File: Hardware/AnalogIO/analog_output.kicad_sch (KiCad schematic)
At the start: 18 parts, among them U23 MCP6002-xSN, U24 MCP6002-xSN, U4 MCP6002-xSN, U5 MCP6002-xSN

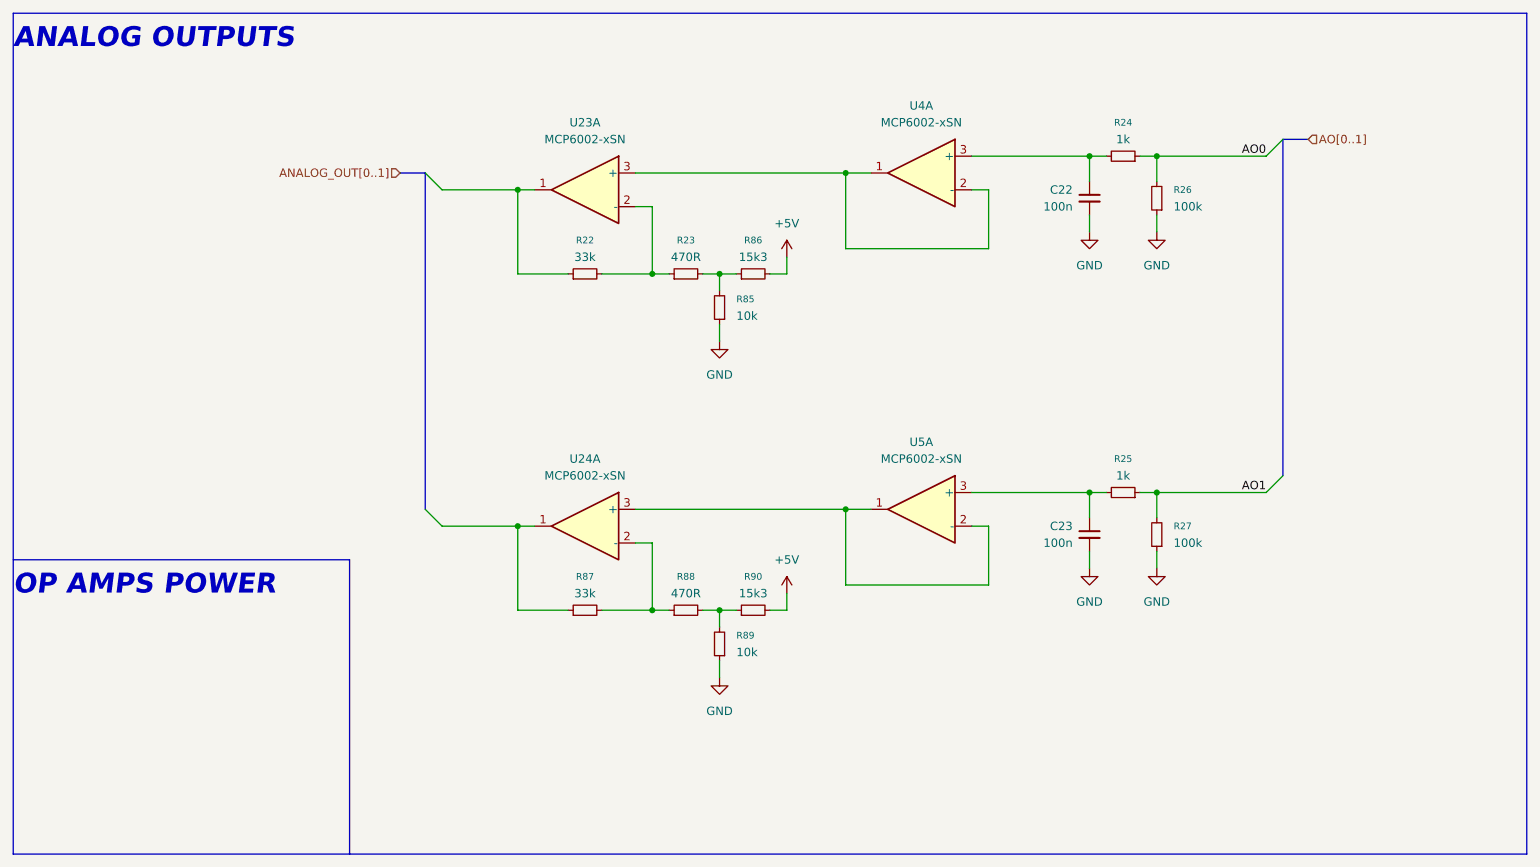
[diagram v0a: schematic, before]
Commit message: schematic update - all pcbs
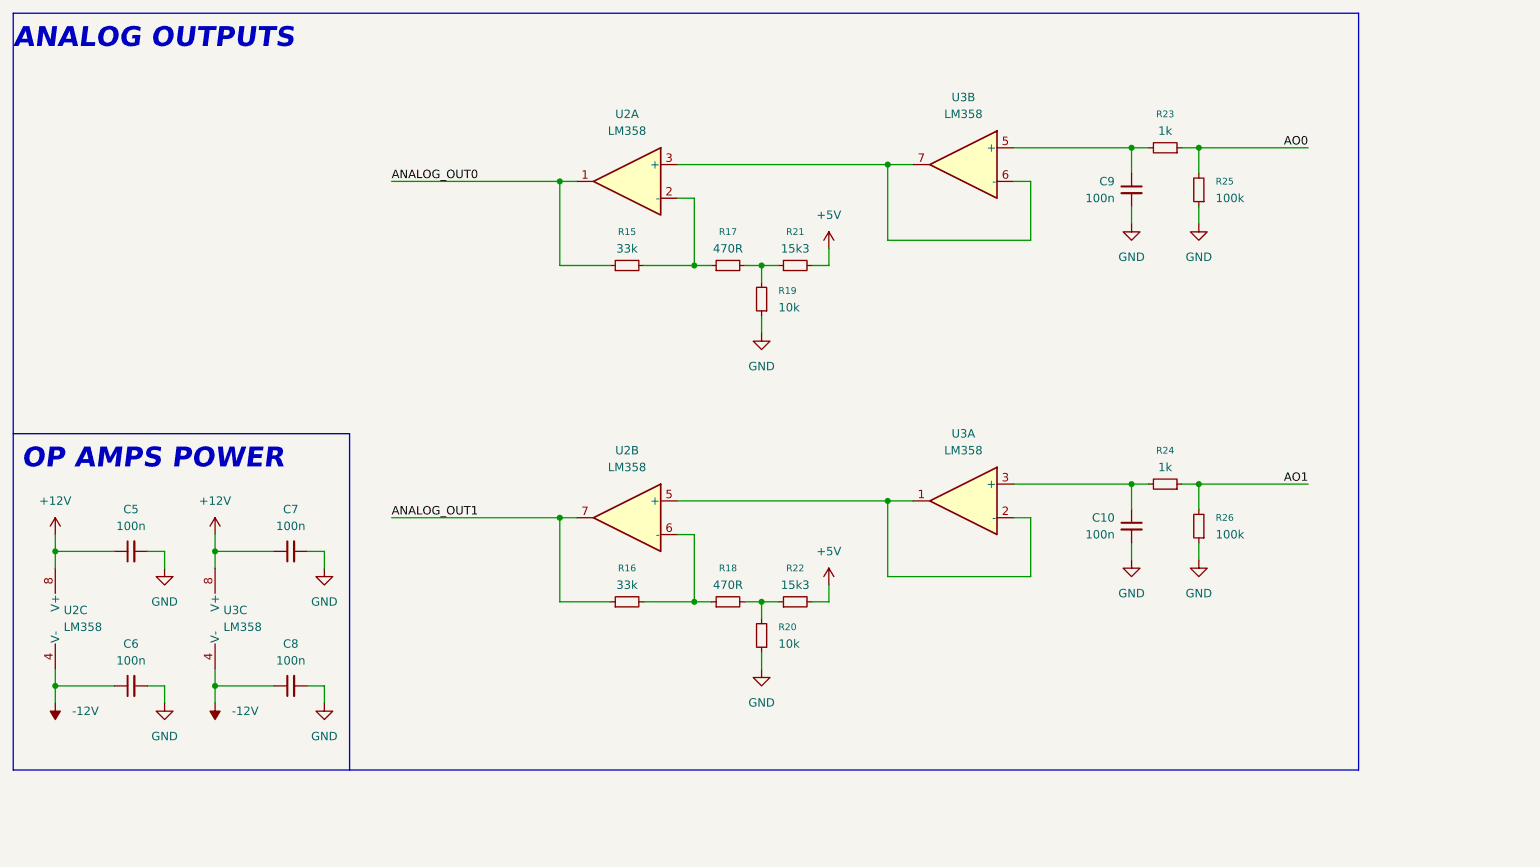
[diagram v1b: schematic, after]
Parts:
- removed U23, U24, U4: MCP6002-xSN, Package_SO:SOIC-8_3.9x4.9mm_P1.27mm, symbol Amplifier_Operational:MCP6002-xSN
- removed U5: MCP6002-xSN, symbol Amplifier_Operational:MCP6002-xSN
- added C5, C6, C7, C8: 100n, symbol Device:C_Small
- added U2, U3: LM358, symbol Amplifier_Operational:LM358
- renumbered C23 to C10, C22 to C9, R22 to R15, R87 to R16, R23 to R17, R88 to R18, R85 to R19, R89 to R20, R86 to R21, R90 to R22, R24 to R23, R25 to R24, R26 to R25, R27 to R26
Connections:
- net GND: now also C5.2, C6.2, C7.2, C8.2
- net at R15.2, R17.1: now also U2.2 (-)
- net ANALOG_OUT0: now reaches R15.1
- net ANALOG_OUT0: now also U2.1
- net at C10.1, R24.2: now also U3.3 (+)
- net at C9.1, R23.2: now also U3.5 (+)
- net ANALOG_OUT1: now reaches R16.1
- net ANALOG_OUT1: now also U2.7
- net at R16.2, R18.1: now also U2.6 (-)
- new net: U2.5 (+), U3.1, U3.2 (-)
- new net: U2.3 (+), U3.6 (-), U3.7
- new net +12V: C5.1, C7.1, U2.8 (V+), U3.8 (V+)
- new net -12V: C6.1, C8.1, U2.4 (V-), U3.4 (V-)
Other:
- moved on the sheet: C10, C9, R15, R16, R17, R18, R19, R20, R21, R22, R23, R24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

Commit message: schematic update - digital and analog footprints added
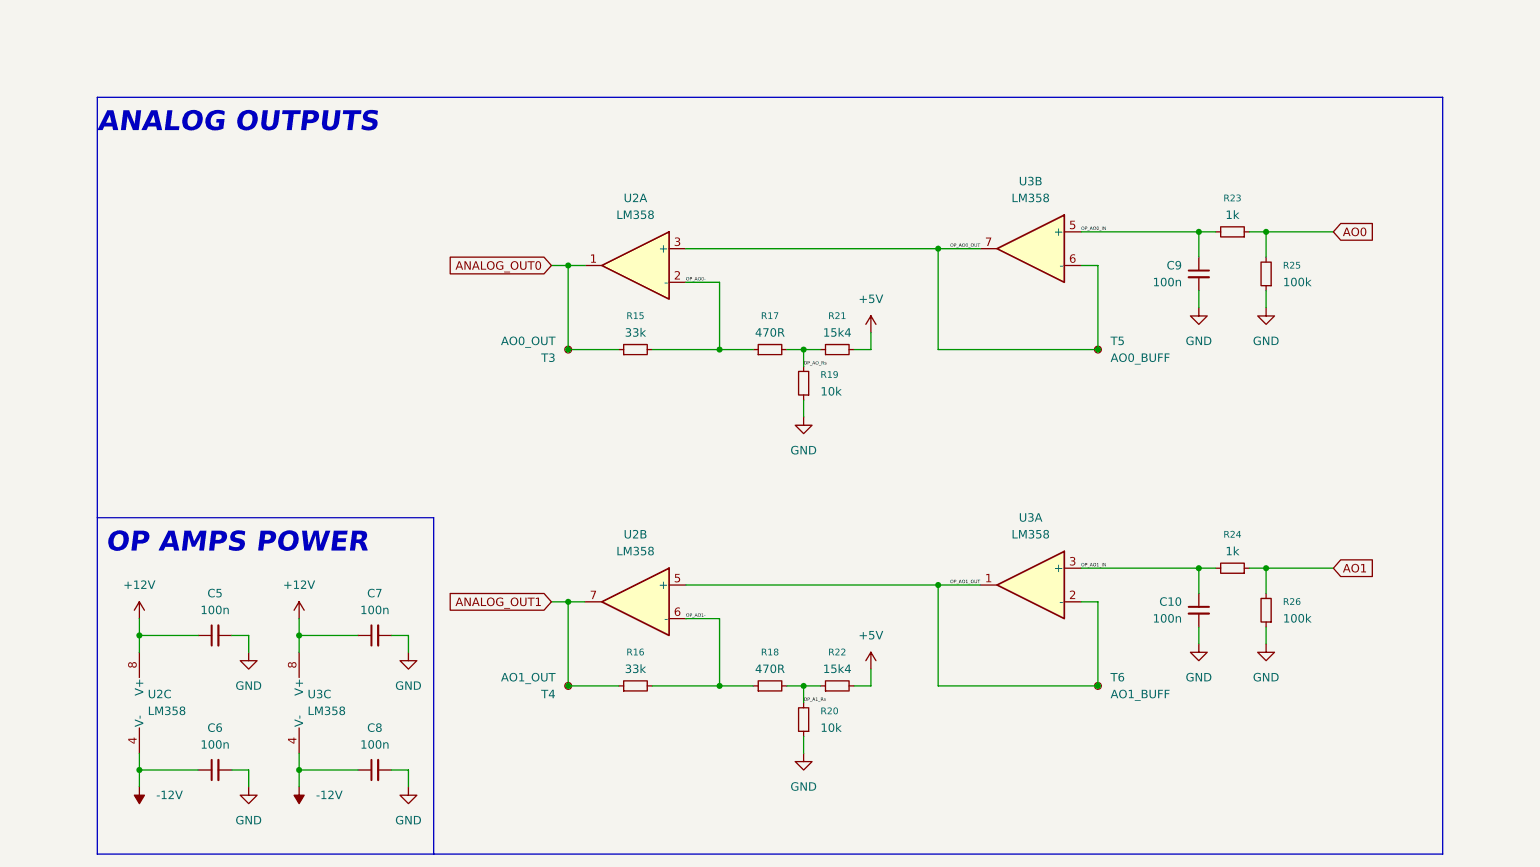
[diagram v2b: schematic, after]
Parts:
- added T3: AO0_OUT, TestPoint:TestPoint_Pad_1.0x1.0mm, symbol Connector:TestPoint_Small
- added T4: AO1_OUT, TestPoint:TestPoint_Pad_1.0x1.0mm, symbol Connector:TestPoint_Small
- added T5: AO0_BUFF, TestPoint:TestPoint_Pad_1.0x1.0mm, symbol Connector:TestPoint_Small
- added T6: AO1_BUFF, TestPoint:TestPoint_Pad_1.0x1.0mm, symbol Connector:TestPoint_Small
- C5, C6, C7, C8: footprint (none) -> Capacitor_SMD:C_0603_1608Metric_Pad1.08x0.95mm_HandSolder; Mouser Part Number (none) -> GRM033R6YA104ME14D; Mouser Price/Stock (none) -> https://www.mouser.pl/ProductDetail/Murata-Electronics/GRM0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
- R15, R16: footprint (none) -> Resistor_SMD:R_0603_1608Metric_Pad0.98x0.95mm_HandSolder; Mouser Part Number (none) -> 71-CRCW0603-33K-E3; Mouser Price/Stock (none) -> https://www.mouser.pl/ProductDetail/Vishay/CRCW060333K0FKEA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
- R17, R18: footprint (none) -> Resistor_SMD:R_0603_1608Metric_Pad0.98x0.95mm_HandSolder; Mouser Part Number (none) -> 71-CRCW0603-470-E3; Mouser Price/Stock (none) -> https://www.mouser.pl/ProductDetail/Vishay/CRCW0603470RFKEA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
- R19, R20: footprint (none) -> Resistor_SMD:R_0603_1608Metric_Pad0.98x0.95mm_HandSolder; Mouser Part Number (none) -> 71-CRCW0603-10K-E3; Mouser Price/Stock (none) -> https://www.mouser.pl/ProductDetail/Vishay/CRCW060310K0FKEA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
- R21, R22: value 15k3 -> 15k4; footprint (none) -> Resistor_SMD:R_0603_1608Metric_Pad0.98x0.95mm_HandSolder; Mouser Part Number (none) -> 71-CRCW0603-15.4K-E3; Mouser Price/Stock (none) -> https://www.mouser.pl/ProductDetail/Vishay/CRCW060315K4FKEA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
- U2, U3: footprint (none) -> Package_SO:SOIC-8_3.9x4.9mm_P1.27mm; Mouser Part Number (none) -> 511-LM358D; Mouser Price/Stock (none) -> https://www.mouser.pl/ProductDetail/STMicroelectronics/LM35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
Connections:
- net ANALOG_OUT0: now also T3.1
- net ANALOG_OUT1: now also T4.1
- net OP_AO0-: now reaches R15.2, R17.1, U2.2 (-)
- net OP_AO_Rs: now reaches R17.2, R19.2, R21.1
- net OP_AO1_OUT: now reaches U2.5 (+), U3.1, U3.2 (-)
- net OP_AO1_OUT: now also T6.1
- net OP_AO1-: now reaches R16.2, R18.1, U2.6 (-)
- net OP_AO1_IN: now reaches C10.1, R24.2, U3.3 (+)
- net OP_A1_Rs: now reaches R18.2, R20.2, R22.1
- net OP_AO0_IN: now reaches C9.1, R23.2, U3.5 (+)
- net OP_AO0_OUT: now reaches U2.3 (+), U3.6 (-), U3.7
- net OP_AO0_OUT: now also T5.1
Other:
- moved on the sheet: C10, C5, C6, C7, C8, C9, R15, R16, R17, R18, R19, R20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

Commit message: schematic update & pcb update
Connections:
- net ANALOG_OUT0: now also U2.7; no longer U2.1
- net ANALOG_OUT1: now also U2.1; no longer U2.7
- net OP_AO0-: now also U2.6 (-); no longer U2.2 (-)
- net OP_AO0_OUT: now also U2.5 (+); no longer U2.3 (+)
- net OP_AO1-: now also U2.2 (-); no longer U2.6 (-)
- net OP_AO1_OUT: now also U2.3 (+); no longer U2.5 (+)
- net +12V renamed +15V
- net -12V renamed -15V
- net AO0 renamed AO_0
- net AO1 renamed AO_1
